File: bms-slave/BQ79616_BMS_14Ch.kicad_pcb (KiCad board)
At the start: 4 copper layers, 140 x 70 mm, 180 parts, among them J1 Conn_Therm, J2 Conn_02x10_Odd_Even, J3 Conn_02x10_Odd_Even, J4 BMS_A_OUT, J5 BMS_A_IN, Q1 MMBT5551, Q10 DMN2024UQ, Q11 DMN2024UQ, Q12 DMN2024UQ, Q13 DMN2024UQ, Q14 DMN2024UQ, Q15 DMN2024UQ, Q2 DMN2024UQ, Q3 DMN2024UQ, Q4 DMN2024UQ, Q5 DMN2024UQ, Q6 DMN2024UQ, Q7 DMN2024UQ, Q8 DMN2024UQ, Q9 DMN2024UQ

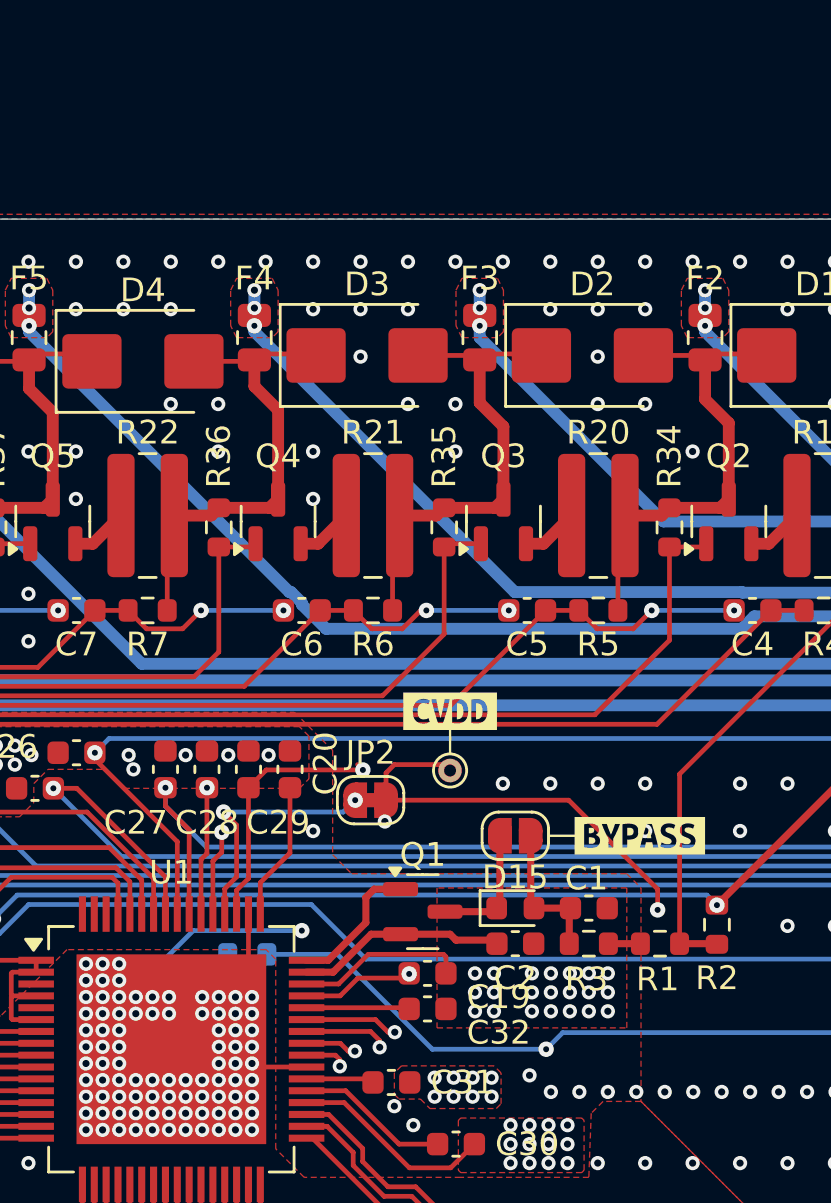
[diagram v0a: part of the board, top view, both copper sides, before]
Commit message: fix: use DXT5551P5 to increase power and remove onboard NTC
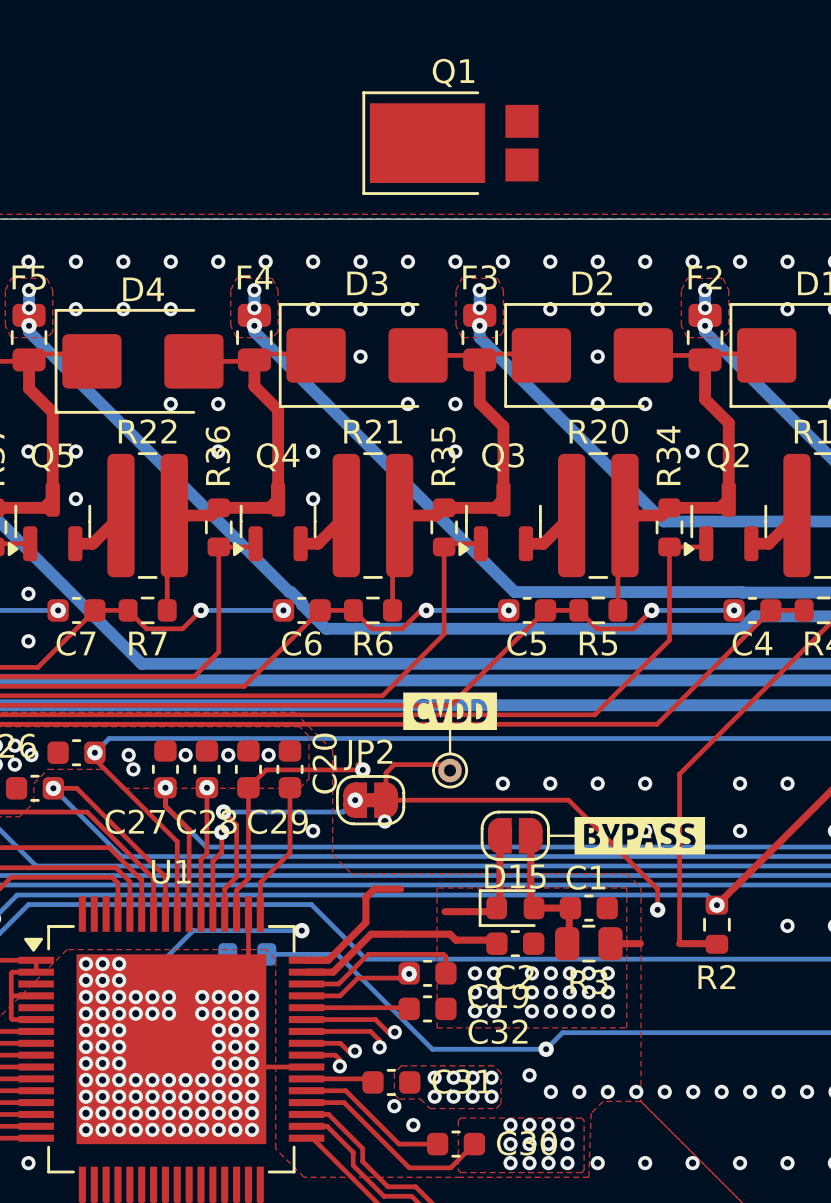
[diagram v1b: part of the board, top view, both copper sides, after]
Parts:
- removed R1: 200R, Resistor_SMD:R_0603_1608Metric
- removed TH8: onboard_10k_NTC, Resistor_SMD:R_0603_1608Metric
- Q1: value MMBT5551 -> DXT5551P5; footprint Package_TO_SOT_SMD:SOT-23 -> Diode_SMD:D_PowerDI-5
- R3: footprint Resistor_SMD:R_0603_1608Metric -> Resistor_SMD:R_0805_2012Metric
- moved Q1 32.4 mm to (161.9, 56.8)
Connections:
- J1 pad 17: unconnected-(J1-Pin_17-Pad17) -> /TH_A8
- Q1 pad 1: /NPNB_A -> Net-(D15-K)
- Q1 pad 2: /LDOIN_A -> /NPNB_A
- Q1 pad 3: Net-(D15-K) -> /LDOIN_A
- R3 pad 1: Net-(R1-Pad2) -> Net-(D1-A2)
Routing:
- net Net-(R1-Pad2): track 1.35 -> 0.00 mm
- net Net-(D1-A2): track 38.3 -> 39.6 mm

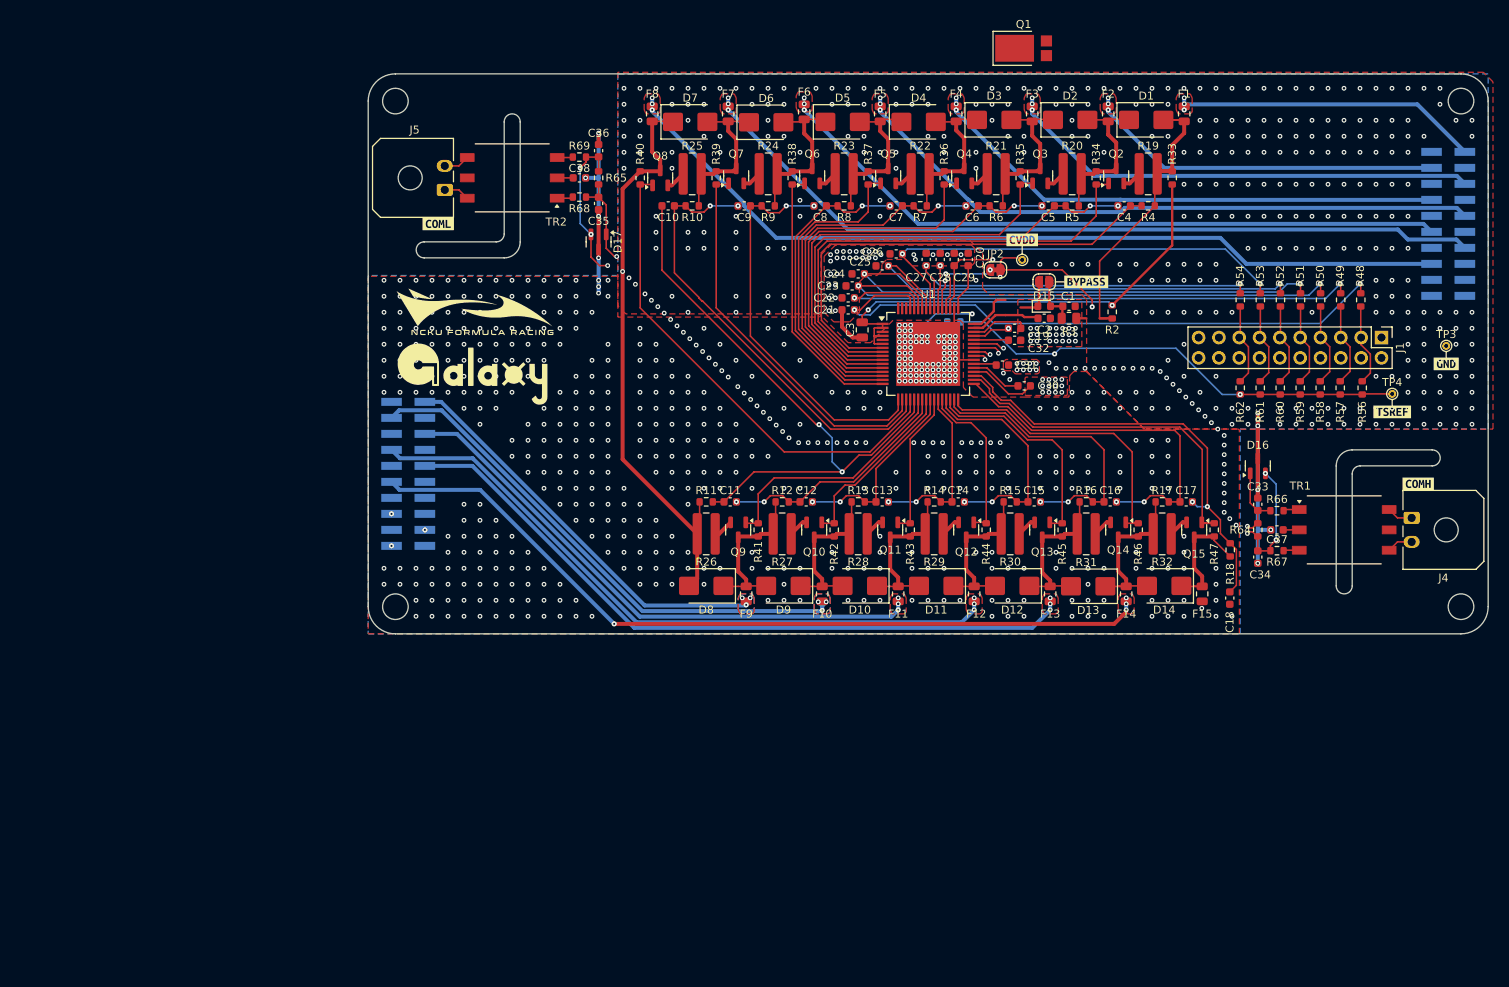
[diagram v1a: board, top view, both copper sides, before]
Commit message: feat: bms slave layout
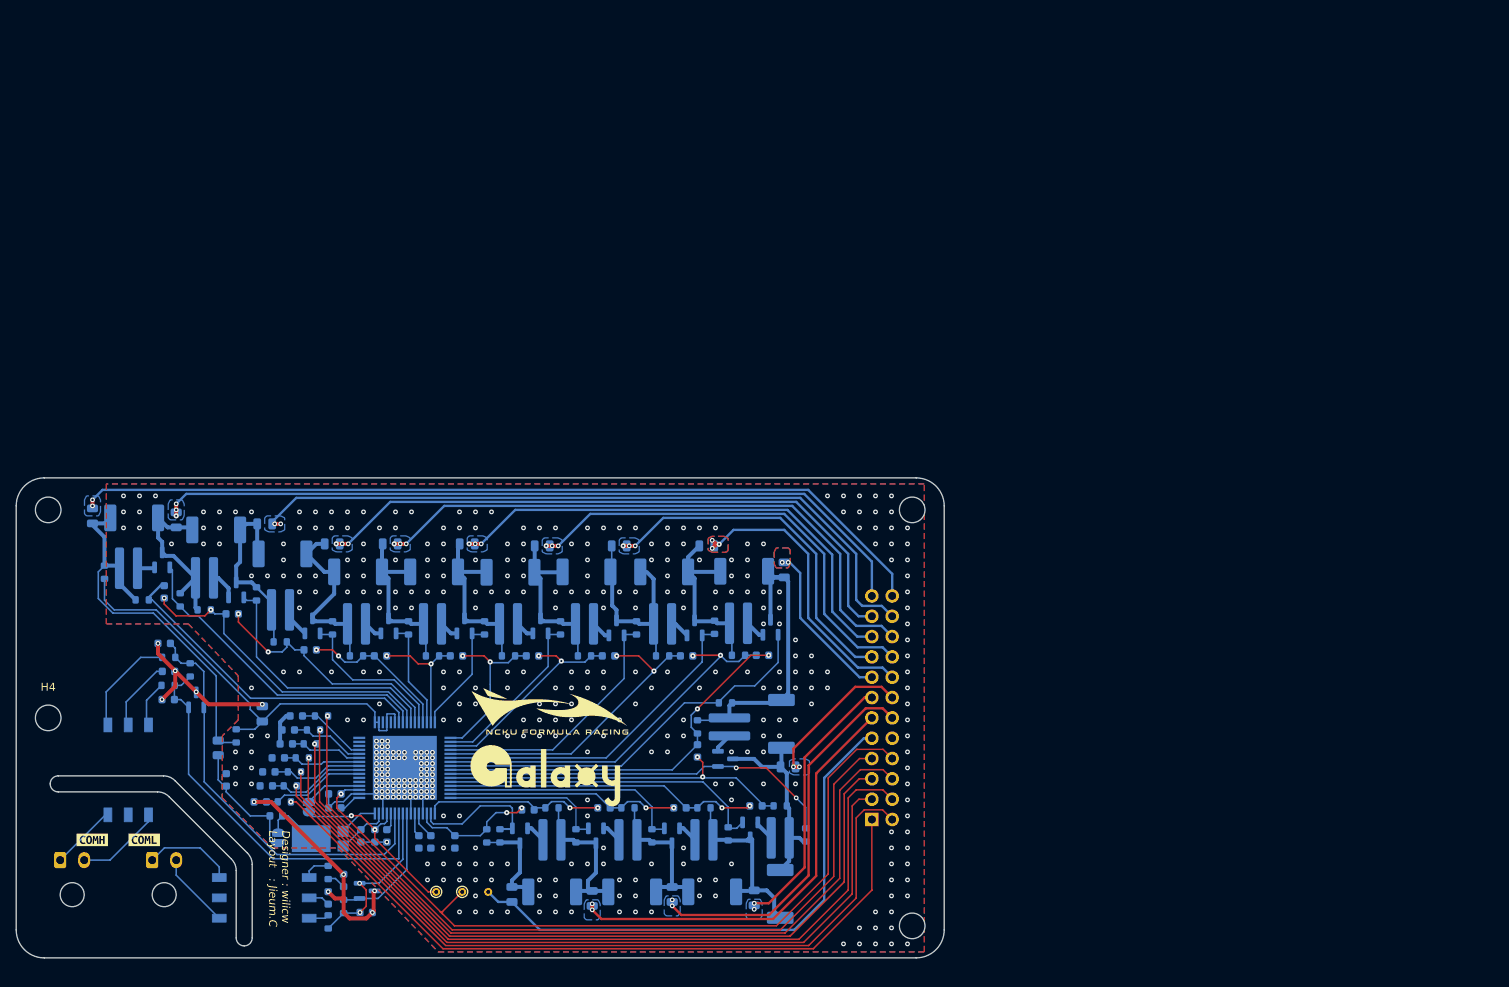
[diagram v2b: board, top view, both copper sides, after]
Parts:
- removed C28: 100n, Capacitor_SMD:C_0603_1608Metric
- removed J1: Conn_Therm, Connector_PinHeader_2.54mm:PinHeader_2x10_P2.54mm_Vertical
- removed J3: Conn_02x10_Odd_Even, Connector_PinHeader_2.00mm:PinHeader_2x10_P2.00mm_Vertical_SMD
- removed R55: 1k, Resistor_SMD:R_0603_1608Metric
- removed R56, R57, R58, R59, R60, R61, R62, R63: 10k, Resistor_SMD:R_0603_1608Metric
- removed kibuzzard-67C80B11: G***, kibuzzard-67C80B11
- removed kibuzzard-67C80BF3: G***, kibuzzard-67C80BF3
- removed kibuzzard-67C80C10: G***, kibuzzard-67C80C10
- removed kibuzzard-67C80F0F: G***, kibuzzard-67C80F0F
- added kibuzzard-67C80B29: G***, kibuzzard-67C80B29, B.Cu at (56.8, 155.8)
- added kibuzzard-69D6BEF3: G***, kibuzzard-69D6BEF3, F.Cu at (45.5, 155.8)
- added kibuzzard-69D6BEF3: G***, kibuzzard-69D6BEF3, B.Cu at (41.0, 155.8)
- added kibuzzard-69DFF7FB: G***, kibuzzard-69DFF7FB, B.Cu at (91.8, 164.5)
- added kibuzzard-69DFF833: G***, kibuzzard-69DFF833, B.Cu at (96.2, 164.5)
- added kibuzzard-69E0451B: G***, kibuzzard-69E0451B, B.Cu at (100.5, 139.0)
- C1, C10, C11, C12, C13, C14, C15, C16, C17, C18, C19, C2, C20, C21, C22, C23, C24, C25, C26, C27, C29, C3, C30, C31, C32, C33, C34, C35, C36, C37, C38, C4, C5, C6, C7, C8, C9, D15, D16, D17, F1, F10, F11, F12, F13, F14, F15, F2, F3, F4, F5, F6, F7, F8, F9, J4, J5, JP1, JP2, Q1, Q10, Q11, Q12, Q13, Q14, Q15, Q2, Q3, Q4, Q5, Q6, Q7, Q8, Q9, R10, R11, R12, R13, R14, R15, R16, R17, R18, R19, R2, R20, R21, R22, R23, R24, R25, R26, R27, R28, R29, R3, R30, R31, R32, R33, R34, R35, R36, R37, R38, R39, R4, R40, R41, R42, R43, R44, R45, R46, R47, R48, R49, R5, R50, R51, R52, R53, R54, R6, R64, R65, R66, R67, R68, R69, R7, R8, R9, TP3, TR1, TR2, U1, kibuzzard-67C80B8B: moved to B.Cu
- D1, D10, D11, D12, D13, D14, D2, D3, D4, D5, D6, D7, D8, D9: footprint Diode_SMD:D_SMB -> Fuse:Fuse_2512_6332Metric_Pad1.52x3.35mm_HandSolder; moved to B.Cu
- J2: value Conn_02x10_Odd_Even -> Conn_02x12_Odd_Even; footprint Connector_PinHeader_2.00mm:PinHeader_2x10_P2.00mm_Vertical_SMD -> Connector_PinHeader_2.54mm:PinHeader_2x12_P2.54mm_Horizontal
- moved H4 177.1 mm to (40.0, 140.5)
- moved J4 174.3 mm to (41.5, 158.3), turned to 0 degrees
- moved TR1 154.9 mm to (50.0, 147.0), turned to -90 degrees
- moved F1 145.4 mm to (45.5, 115.2)
- moved R33 142.3 mm to (47.0, 122.3)
- moved R48 139.9 mm to (74.2, 140.3), turned to 0 degrees
- moved R66 139.7 mm to (55.1, 132.9), turned to 180 degrees
- moved C37 139.7 mm to (55.0, 134.7), turned to 0 degrees
- moved R67 139.6 mm to (55.0, 136.4), turned to 180 degrees
- moved R49 139.2 mm to (73.2, 142.0), turned to 0 degrees
- moved R50 137.9 mm to (72.8, 143.8), turned to 0 degrees
- moved TP3 137.8 mm to (95.0, 162.2), turned to 180 degrees
- moved C33 137.8 mm to (54.5, 131.2), turned to 180 degrees
- moved C34 137.4 mm to (55.0, 138.2), turned to 180 degrees
- moved R51 137.3 mm to (71.8, 145.5), turned to 0 degrees
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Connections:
- J2 pad 1: /CELL_A14 -> /NTC07
- J2 pad 10: unconnected-(J2-Pin_10-Pad10) -> GND1
- J2 pad 11: unconnected-(J2-Pin_11-Pad11) -> /CELL_A1
- J2 pad 12: /CELL_A9 -> /CELL_A2
- J2 pad 13: /CELL_A8 -> /CELL_A3
- J2 pad 14: unconnected-(J2-Pin_14-Pad14) -> /CELL_A4
- J2 pad 15: unconnected-(J2-Pin_15-Pad15) -> /CELL_A5
- J2 pad 16: /CELL_A7 -> /CELL_A6
- J2 pad 17: unconnected-(J2-Pin_17-Pad17) -> /CELL_A7
- J2 pad 18: unconnected-(J2-Pin_18-Pad18) -> /CELL_A8
- J2 pad 19: unconnected-(J2-Pin_19-Pad19) -> /CELL_A9
- J2 pad 2: unconnected-(J2-Pin_2-Pad2) -> /NTC06
- J2 pad 20: unconnected-(J2-Pin_20-Pad20) -> /CELL_A10
- J2 pad 3: unconnected-(J2-Pin_3-Pad3) -> /NTC05
- J2 pad 4: /CELL_A13 -> /NTC04
- J2 pad 5: /CELL_A12 -> /NTC03
- J2 pad 6: unconnected-(J2-Pin_6-Pad6) -> /NTC02
- J2 pad 7: unconnected-(J2-Pin_7-Pad7) -> /NTC01
- J2 pad 8: /CELL_A11 -> /TSREF_A
- J2 pad 9: /CELL_A10 -> GND1
- R48 pad 2: /TH_A1 -> /NTC01
- R49 pad 2: /TH_A2 -> /NTC02
- R50 pad 2: /TH_A3 -> /NTC03
- R51 pad 2: /TH_A4 -> /NTC04
- R52 pad 2: /TH_A5 -> /NTC05
- R53 pad 2: /TH_A6 -> /NTC06
- R54 pad 2: /TH_A7 -> /NTC07
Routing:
- net /NTC02: track 0.00 -> 102.7 mm, vias 0 -> 1
- net /NTC01: track 0.00 -> 101.4 mm, vias 0 -> 1
- net /NTC04: track 0.00 -> 100.4 mm, vias 0 -> 1
- net /CVDD_A: track 122.9 -> 23.2 mm, vias 4 -> 2
- net /NTC03: track 0.00 -> 98.4 mm, vias 0 -> 1
- net /NTC06: track 0.00 -> 97.0 mm, vias 0 -> 1
- net /NTC05: track 0.00 -> 95.9 mm, vias 0 -> 1
- net /NTC07: track 0.00 -> 92.1 mm, vias 0 -> 1
- net /RX_A: track 92.8 -> 7.13 mm, vias 3 -> 0
- net /TX_A: track 83.3 -> 0.00 mm, vias 2 -> 0
- net /COMLN: track 94.2 -> 21.5 mm, vias 4 -> 2
- net /CELL_A14: track 39.0 -> 108.3 mm, vias 3 -> 2
- net /GPIO_A1: track 77.3 -> 8.85 mm, vias 2 -> 0
- net /CELL_A7: track 107.2 -> 44.4 mm
- net /GPIO_A2: track 72.1 -> 9.33 mm, vias 2 -> 0
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- added copper zone on B.Cu, net /CELL_A1
- added copper zone on B.Cu, net /CELL_A10
- added copper zone on B.Cu, net /CELL_A11
- added copper zone on B.Cu, net /CELL_A12
- added copper zone on B.Cu, net /CELL_A13
- added copper zone on B.Cu, net /CELL_A14
- added copper zone on B.Cu, net /CELL_A2
- added copper zone on B.Cu, net /CELL_A3
- added copper zone on B.Cu, net /CELL_A4
- added copper zone on B.Cu, net /CELL_A7
- added copper zone on B.Cu, net /CELL_A8
- added copper zone on B.Cu, net /CELL_A9
- removed copper zone on F.Cu, net /CELL_A1
- removed copper zone on F.Cu, net /CELL_A10
- removed copper zone on F.Cu, net /CELL_A11
- removed copper zone on F.Cu, net /CELL_A12
- removed copper zone on F.Cu, net /CELL_A13
- removed copper zone on F.Cu, net /CELL_A14
- removed copper zone on F.Cu, net /CELL_A2
- removed copper zone on F.Cu, net /CELL_A3
- removed copper zone on F.Cu, net /CELL_A4
- removed copper zone on F.Cu, net /CELL_A7
- removed copper zone on F.Cu, net /CELL_A8
- removed copper zone on F.Cu, net /CELL_A9
- removed copper zone on In1.Cu, net GND1
- removed copper zone on In2.Cu, net GND1
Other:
- board size 140 x 70 mm -> 116 x 60 mm
- board text added: "Designer : wilicw Layout : Jieum.C"

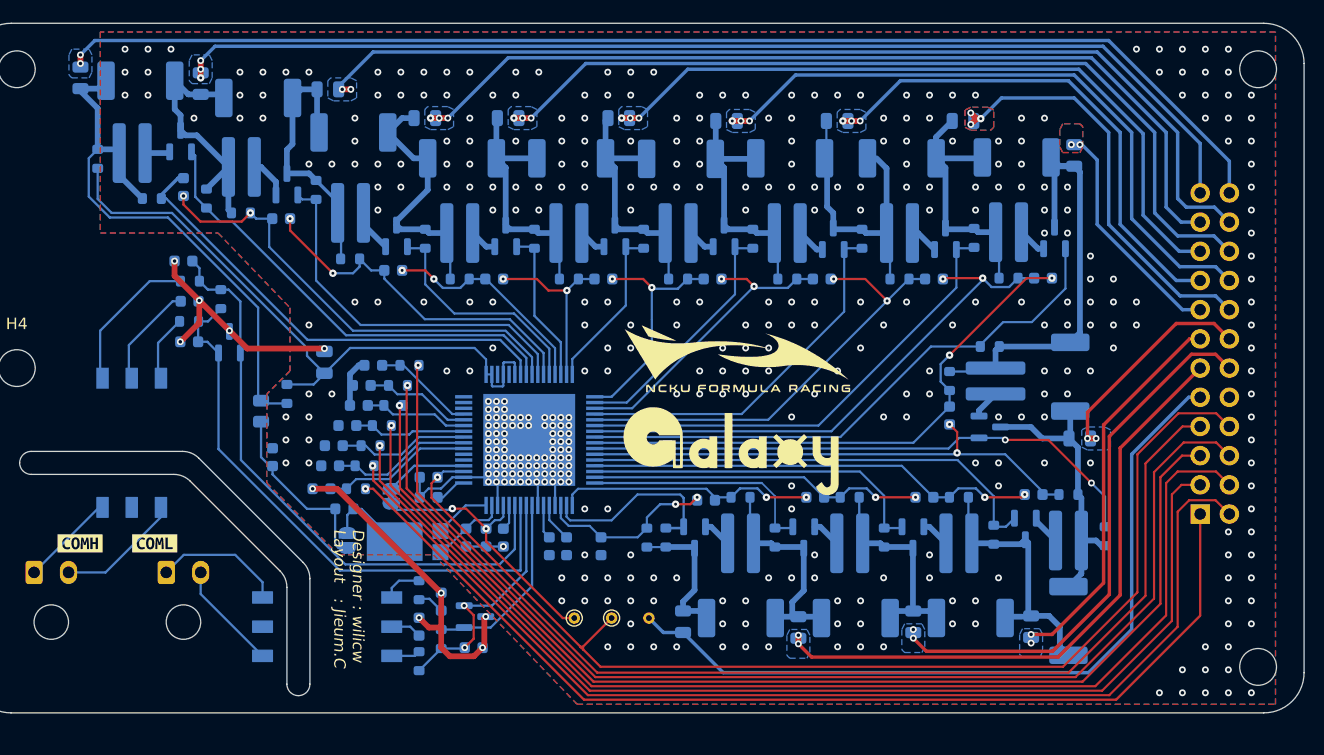
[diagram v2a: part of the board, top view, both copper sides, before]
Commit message: fix: fuse & tvs package
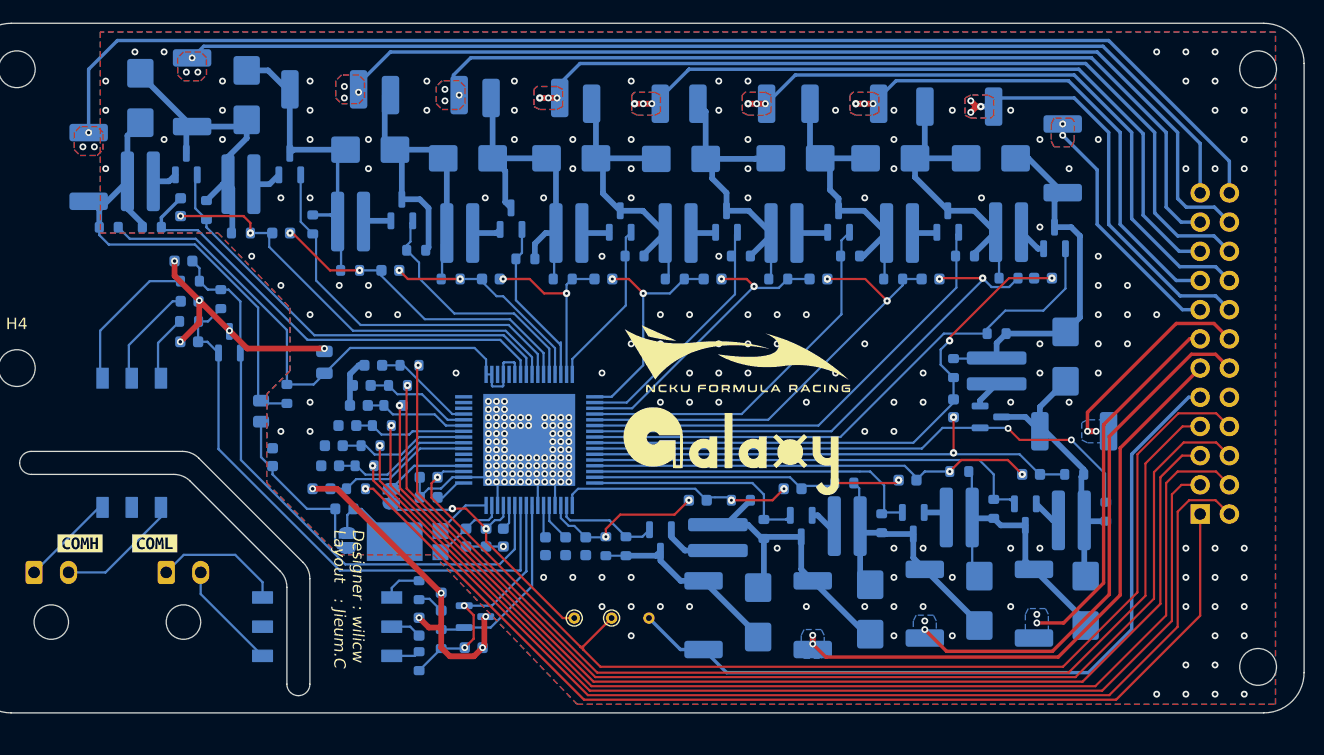
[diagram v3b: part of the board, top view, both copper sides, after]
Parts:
- removed kibuzzard-69E0451B: G***, kibuzzard-69E0451B
- added kibuzzard-69F31310: G***, kibuzzard-69F31310, B.Cu at (100.5, 139.0)
- D1, D10, D11, D12, D13, D14, D2, D3, D4, D5, D6, D7, D8, D9: footprint Fuse:Fuse_2512_6332Metric_Pad1.52x3.35mm_HandSolder -> Diode_SMD:D_SMB
- F1, F10, F11, F12, F13, F14, F15, F2, F3, F4, F5, F6, F7, F8, F9: footprint Fuse:Fuse_0805_2012Metric -> Fuse:Fuse_2512_6332Metric_Pad1.52x3.35mm_HandSolder
- moved F1 7.78 mm to (46.2, 123.0)
- moved R33 6.03 mm to (48.0, 128.2), turned to 0 degrees
- moved R18 3.65 mm to (91.2, 156.0)
- moved R47 3.55 mm to (93.0, 156.0)
- moved R35 3.01 mm to (65.8, 128.0)
- moved Q15 2.98 mm to (96.0, 155.5)
- moved R19 2.56 mm to (50.8, 124.2)
- moved R4 2.50 mm to (51.8, 128.2)
- moved D11 2.30 mm to (133.0, 160.8)
- moved F5 2.30 mm to (84.2, 117.0)
- moved Q4 2.30 mm to (73.5, 126.8)
- moved D9 2.25 mm to (124.8, 122.2)
- moved R44 2.25 mm to (125.0, 152.8)
- moved R15 2.24 mm to (122.0, 149.5)
- moved R30 2.24 mm to (122.0, 153.5)
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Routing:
- net Net-(D3-A1): track 22.5 -> 31.3 mm
- net /CB_A0: track 17.8 -> 9.19 mm
- net Net-(D13-A1): track 18.7 -> 27.2 mm
- net Net-(D12-A1): track 17.7 -> 25.7 mm
- net Net-(D4-A1): track 21.6 -> 29.3 mm
- net /BAT_A: track 56.0 -> 50.0 mm
- net Net-(D1-A2): track 48.7 -> 42.8 mm
- net Net-(D1-A1): track 21.7 -> 27.2 mm
- net Net-(D2-A1): track 21.4 -> 26.7 mm
- net Net-(D14-A1): track 12.4 -> 17.1 mm
- net /CELL_A14: track 108.3 -> 112.9 mm, vias 2 -> 3
- net Net-(D10-A2): track 36.1 -> 31.5 mm
- net Net-(D11-A1): track 22.4 -> 27.0 mm
- net Net-(D8-A1): track 22.5 -> 26.5 mm
- net Net-(D6-A1): track 21.3 -> 25.2 mm
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- added copper zone on F.Cu, net /CELL_A10
- added copper zone on F.Cu, net /CELL_A11
- added copper zone on F.Cu, net /CELL_A12
- added copper zone on F.Cu, net /CELL_A13
- added copper zone on F.Cu, net /CELL_A14
- added copper zone on F.Cu, net /CELL_A7
- added copper zone on F.Cu, net /CELL_A8
- added copper zone on F.Cu, net /CELL_A9
